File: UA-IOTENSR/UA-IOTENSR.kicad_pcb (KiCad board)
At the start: 2 copper layers, 26 parts, among them IC201 BQ2000TPN-B5, J1 Conn_01x04_Male, J201 ZX62-AB-5PA_31_, J202 S2B-ZR-SM4A-TF(LF)(SN), SW1 SW_DPST, U1 ESP32-S3-MINI-1

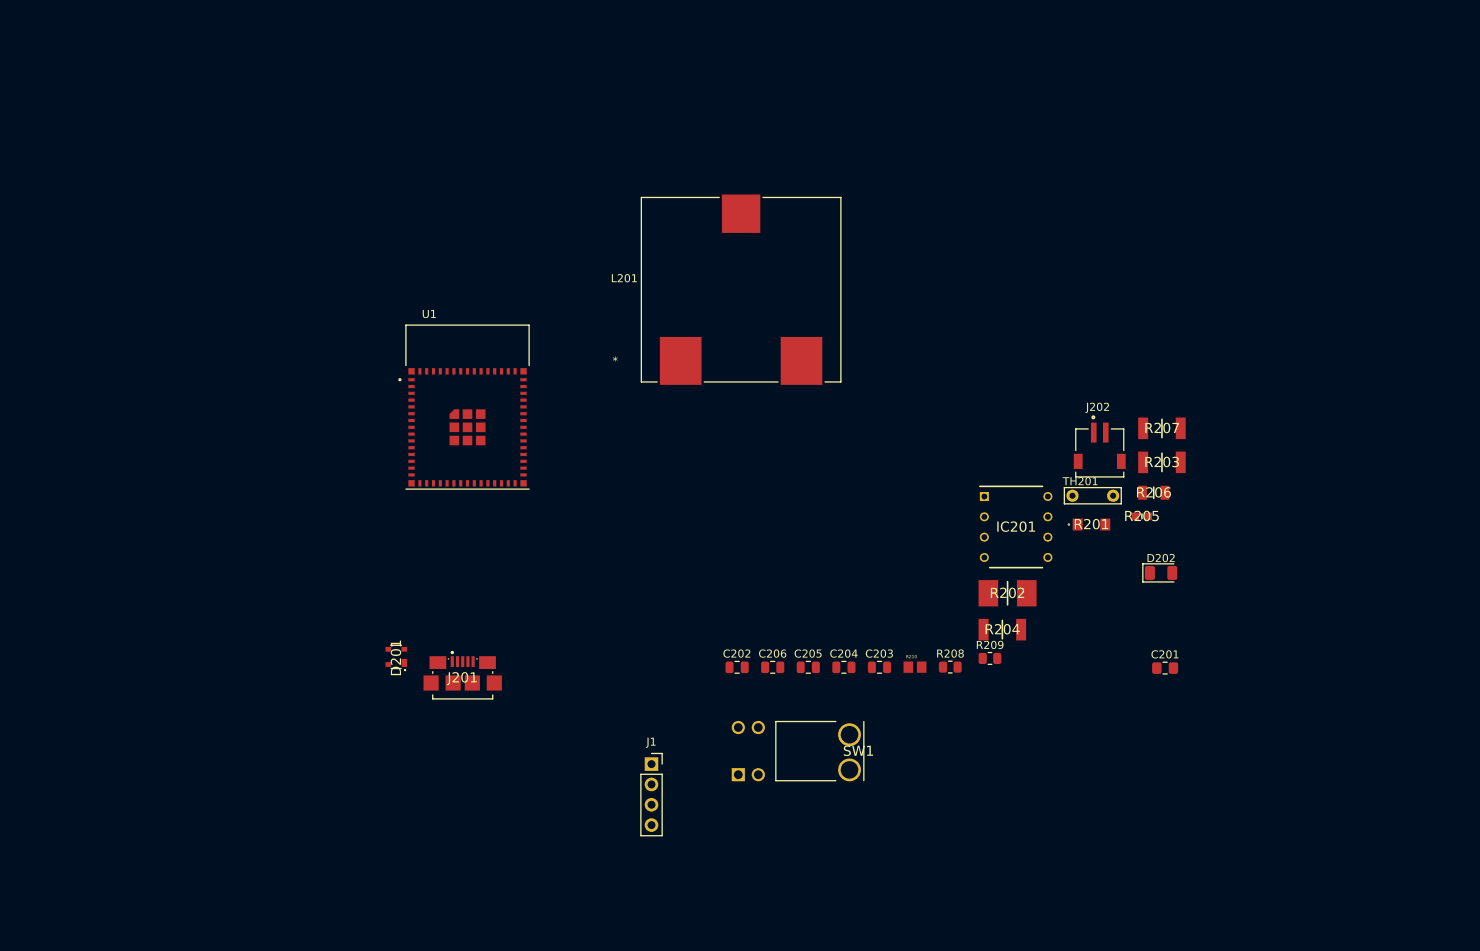
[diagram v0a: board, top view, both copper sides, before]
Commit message: Added 3V3 switch reg with footprint
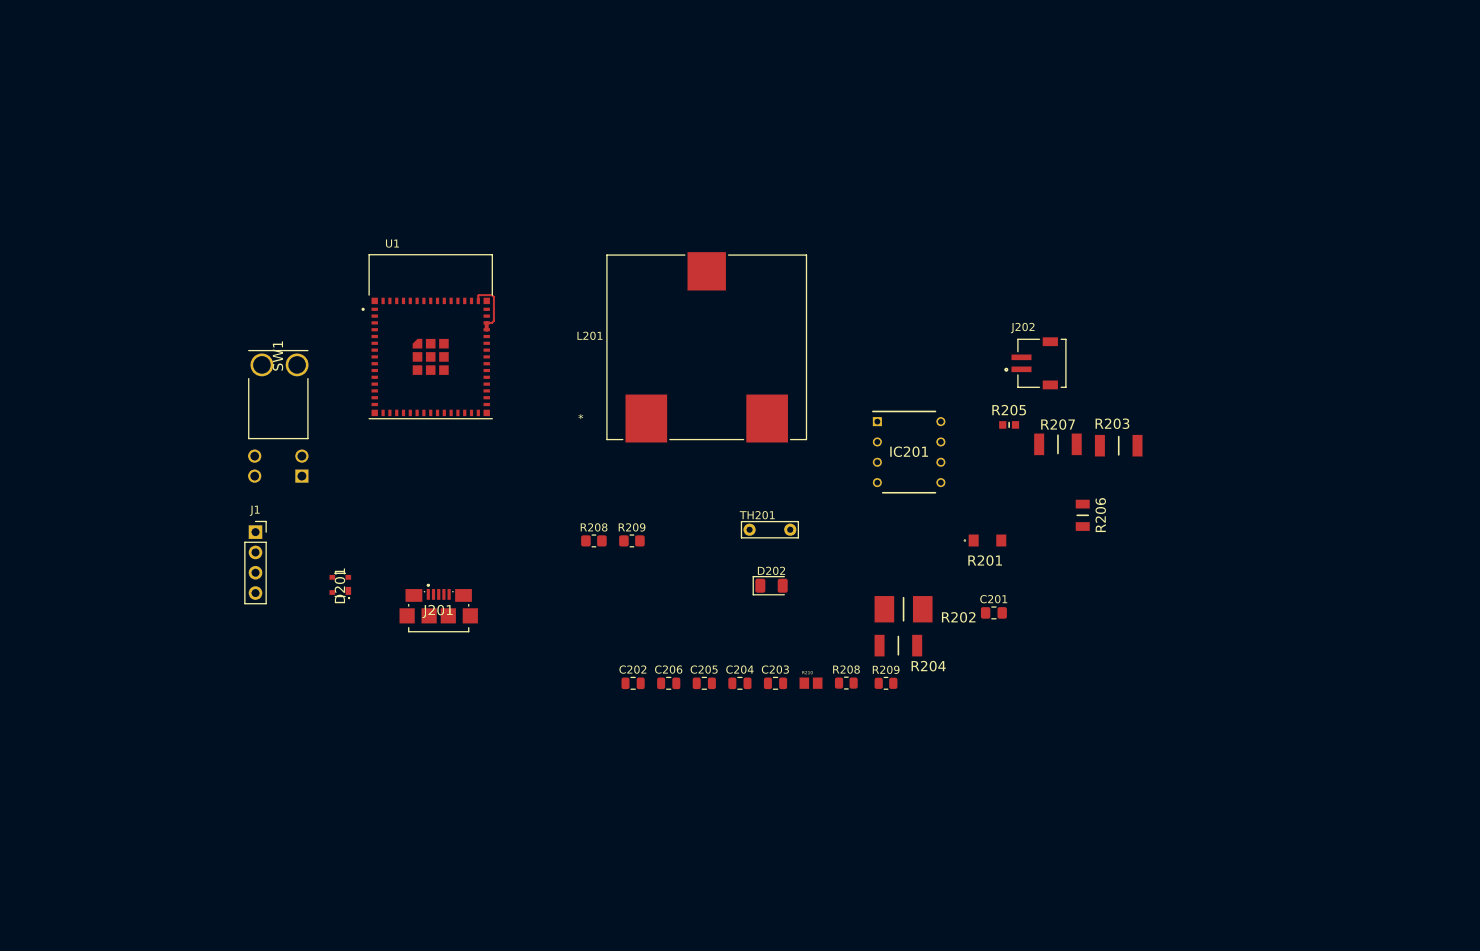
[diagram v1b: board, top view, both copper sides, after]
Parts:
- added R208: 4.8047k, Resistor_SMD:R_0805_2012Metric_Pad1.20x1.40mm_HandSolder, F.Cu at (148.8, 86.3)
- added R209: 5.7668k, Resistor_SMD:R_0805_2012Metric_Pad1.20x1.40mm_HandSolder, F.Cu at (153.6, 86.3)
- moved SW1 66.1 mm to (112.3, 78.2), turned to 90 degrees
- moved J1 57.4 mm to (106.5, 85.2)
- moved D202 48.7 mm to (171.0, 91.9)
- moved TH201 40.6 mm to (170.8, 84.9)
- moved C201 22.5 mm to (198.8, 95.3)
- moved R205 20.2 mm to (200.7, 71.8)
- moved IC201 16.3 mm to (188.2, 75.2)
- moved R209 13.4 mm to (185.3, 104.1)
- moved J202 13.2 mm to (204.4, 64.1), turned to 90 degrees
- moved C202 13.2 mm to (153.7, 104.1)
- moved C203 13.2 mm to (171.5, 104.1)
- moved C204 13.2 mm to (167.1, 104.1)
- moved C205 13.2 mm to (162.6, 104.1)
- moved C206 13.2 mm to (158.2, 104.1)
- moved R201 13.2 mm to (198.0, 86.2)
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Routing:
- net BAT-: track 0.00 -> 7.57 mm

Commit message: Completed regulator circuit; switched to 4-layer board setup
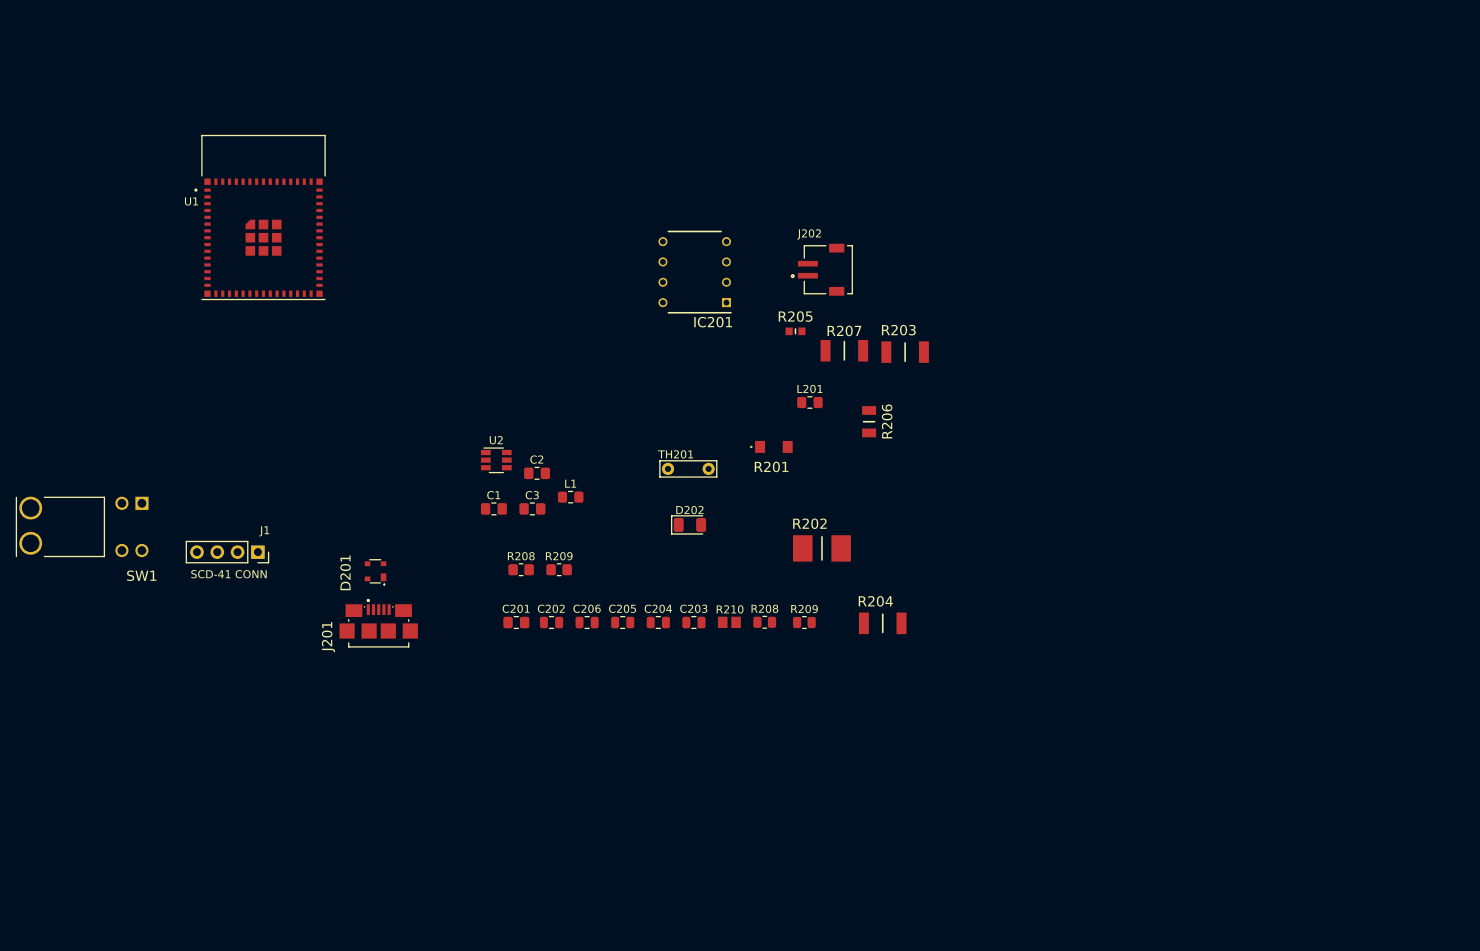
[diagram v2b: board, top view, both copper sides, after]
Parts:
- added C1: 10u, Capacitor_SMD:C_0805_2012Metric_Pad1.18x1.45mm_HandSolder, F.Cu at (136.3, 82.3)
- added C2: 100n, Capacitor_SMD:C_0805_2012Metric_Pad1.18x1.45mm_HandSolder, F.Cu at (141.7, 77.8)
- added C3: 44u, Capacitor_SMD:C_0805_2012Metric_Pad1.18x1.45mm_HandSolder, F.Cu at (141.1, 82.3)
- added L1: 2.2u, Inductor_SMD:L_0805_2012Metric_Pad1.15x1.40mm_HandSolder, F.Cu at (145.9, 80.8)
- added U2: AP63203WU, Package_TO_SOT_SMD:TSOT-23-6, F.Cu at (136.6, 76.2)
- L201: footprint 30u_inductor:B82559A0303A024 -> Inductor_SMD:L_0805_2012Metric_Pad1.15x1.40mm_HandSolder
- moved C201 59.7 mm to (139.1, 96.5)
- moved IC201 35.0 mm to (161.4, 52.7), turned to 180 degrees
- moved R201 29.2 mm to (171.3, 74.5)
- moved R203 29.2 mm to (187.7, 62.7)
- moved R207 29.2 mm to (180.1, 62.5)
- moved J202 29.2 mm to (177.7, 52.4)
- moved R206 29.2 mm to (183.2, 71.4)
- moved R205 29.2 mm to (174.0, 60.1)
- moved U1 25.7 mm to (107.5, 48.4)
- moved SW1 20.3 mm to (92.3, 81.6), turned to 180 degrees
- moved L201 14.6 mm to (175.8, 69.0)
- moved TH201 12.7 mm to (160.6, 77.3)
- moved C204 12.7 mm to (156.8, 96.5)
- moved C206 12.7 mm to (147.9, 96.5)
- moved D202 12.7 mm to (160.8, 84.3)
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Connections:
- J1 pad 3: SCL -> SDA
- J1 pad 4: SDA -> SCL
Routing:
- net BAT-: track 7.57 -> 0.00 mm
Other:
- copper layers 2 -> 4
- board text added: "SCD-41 CONN"

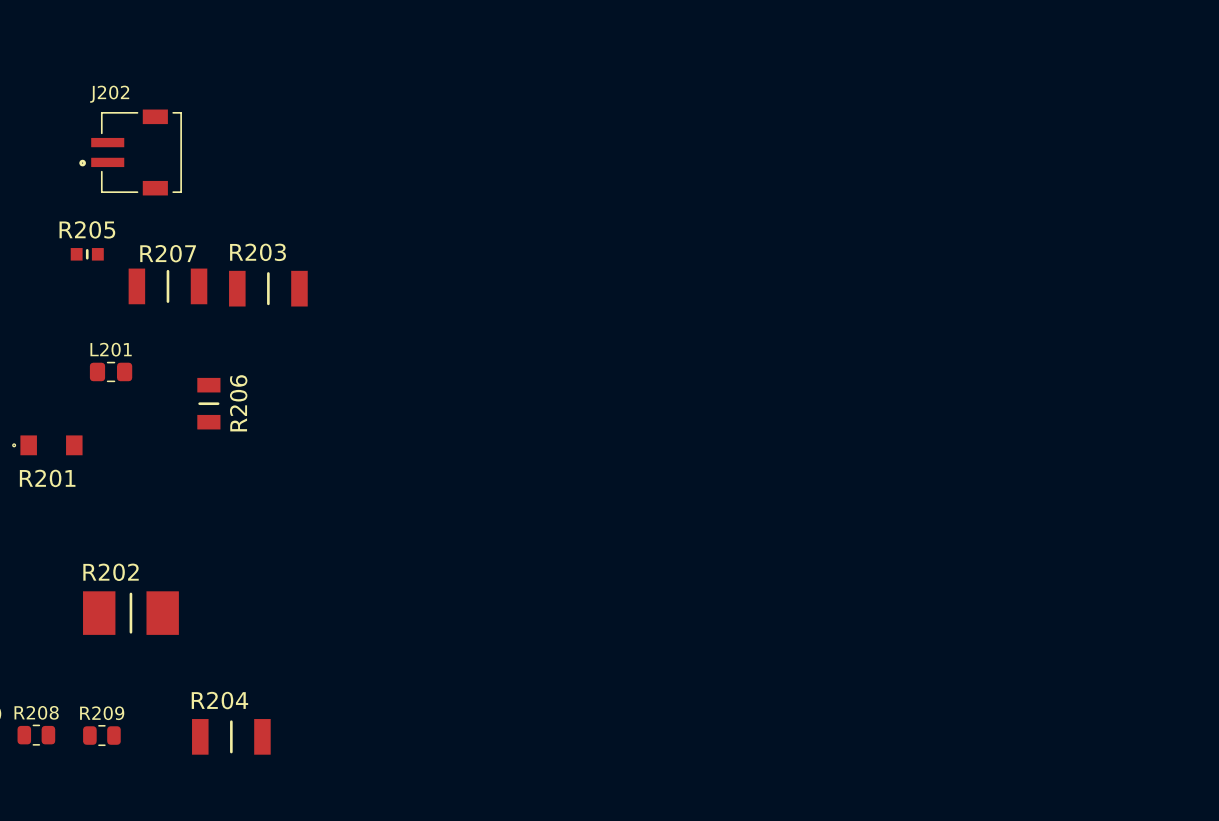
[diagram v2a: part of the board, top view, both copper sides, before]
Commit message: Switched JST Conn to Battery Holder 3x AA
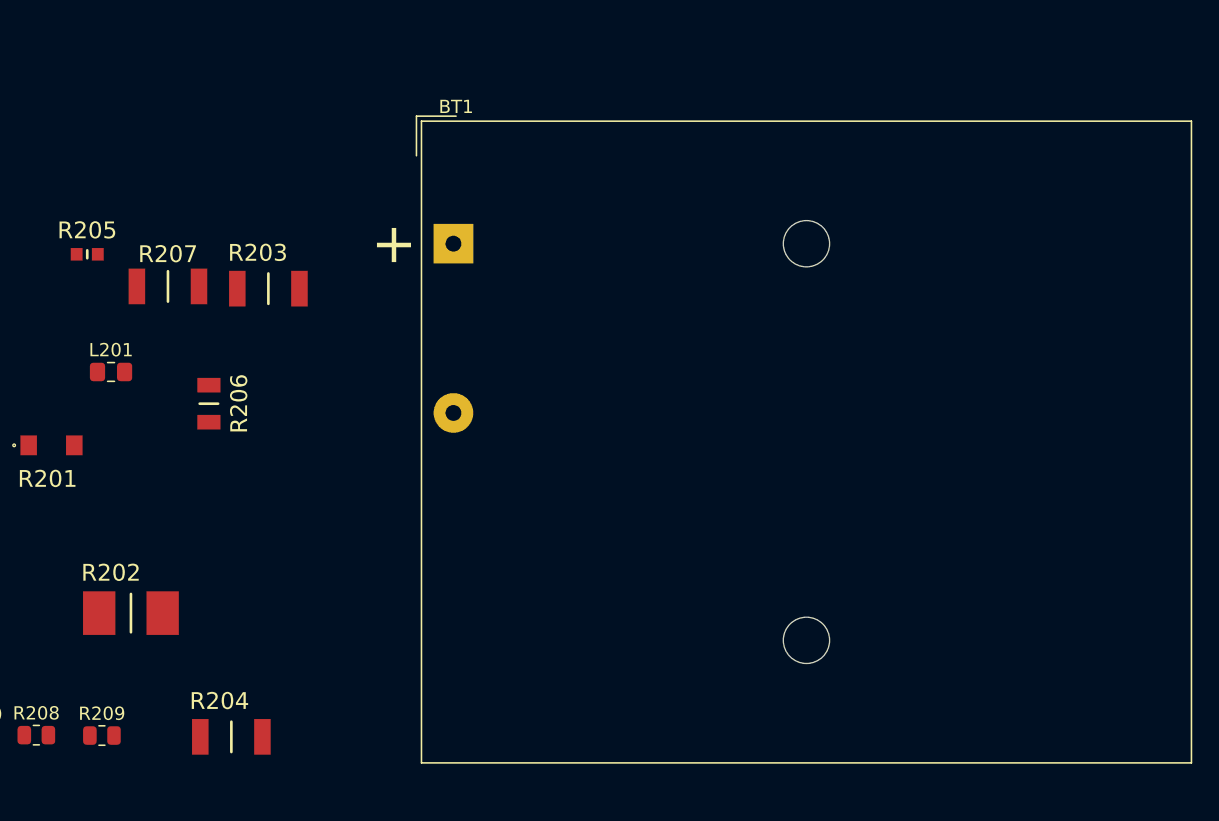
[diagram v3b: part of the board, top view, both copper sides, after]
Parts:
- removed J202: S2B-ZR-SM4A-TF(LF)(SN), JSTConns:JST_S2B-ZR-SM4A-TF(LF)(SN)
- added BT1: Battery, Battery:BatteryHolder_TruPower_BH-331P_3xAA, F.Cu at (201.7, 59.3)

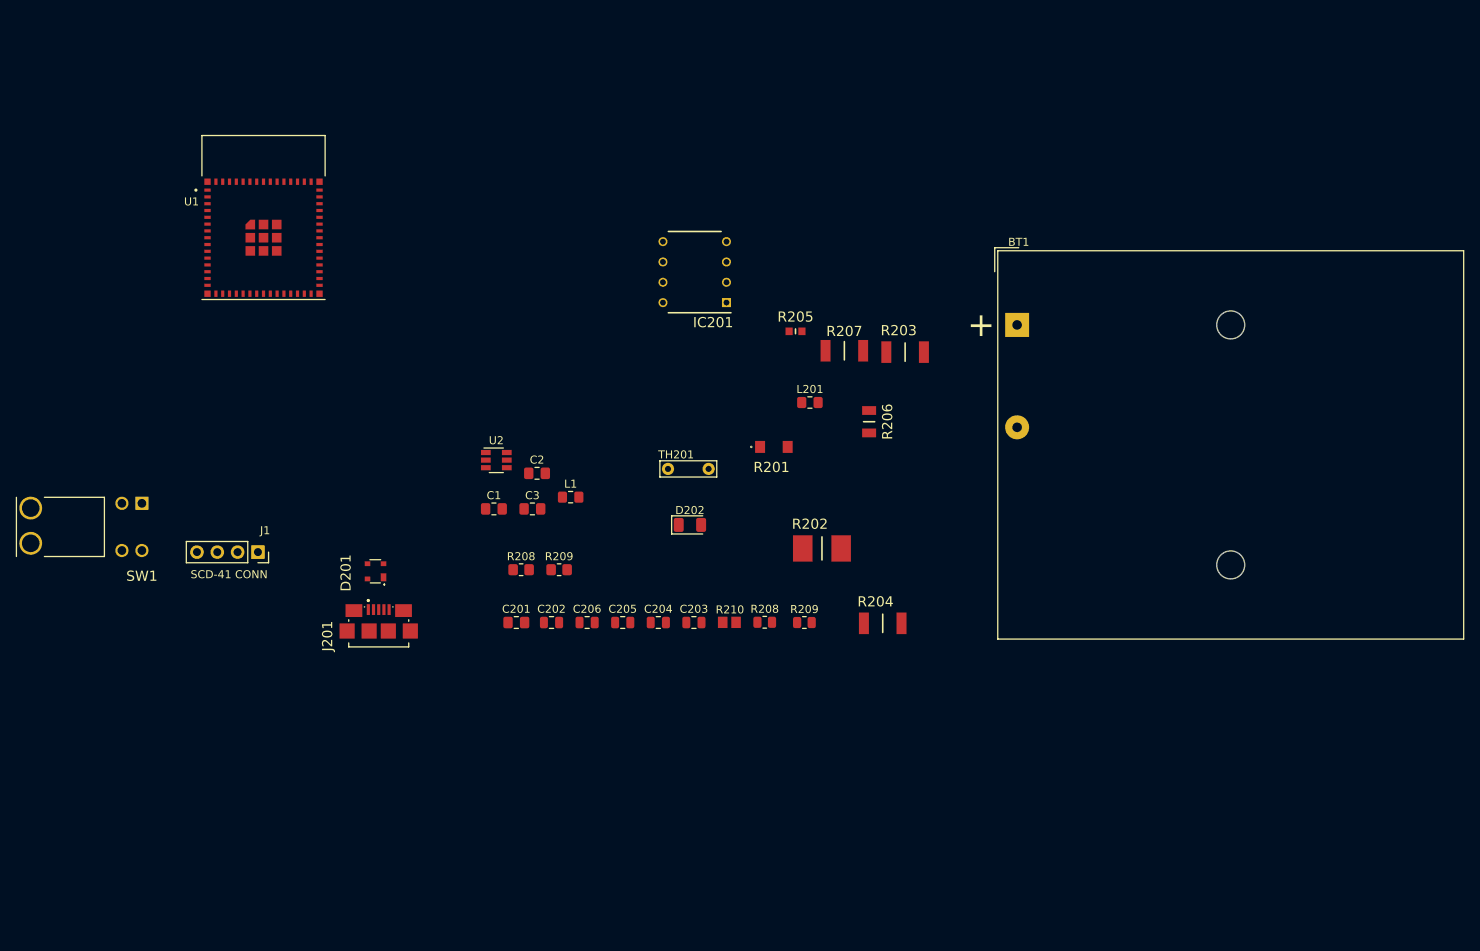
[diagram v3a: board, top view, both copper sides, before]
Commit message: Re-annotated schem, progress on layout
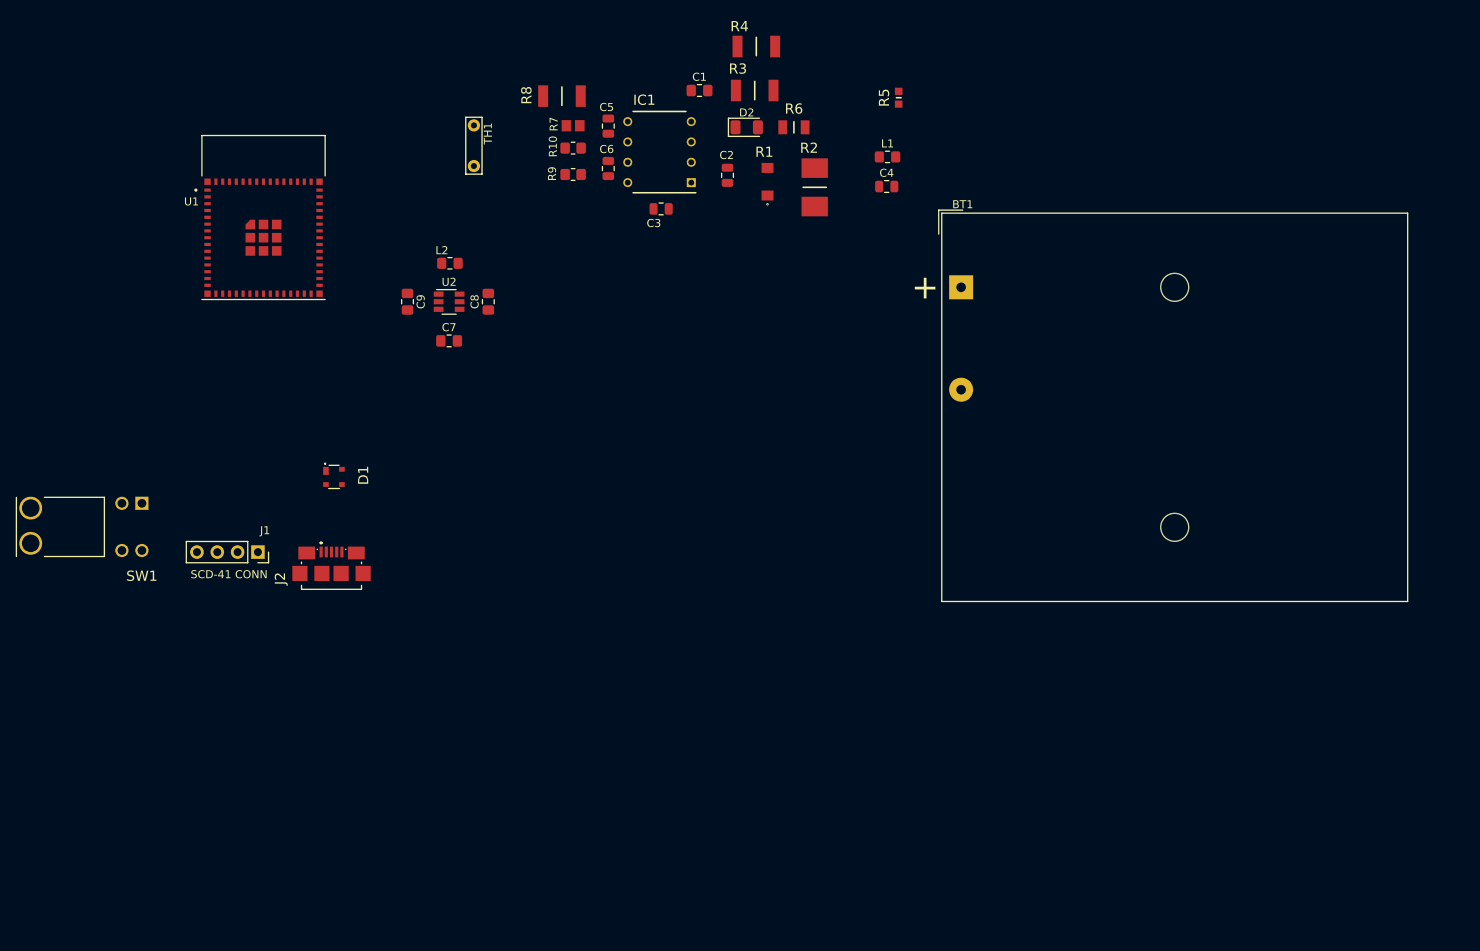
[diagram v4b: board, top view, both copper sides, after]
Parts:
- removed R208: R_T1, Resistor_SMD:R_0805_2012Metric
- removed R209: R_T2, Resistor_SMD:R_0805_2012Metric
- moved R4 73.8 mm to (169.1, 24.5)
- moved C1 70.3 mm to (162.0, 30.0)
- moved R7 65.1 mm to (146.2, 34.4), turned to 180 degrees
- moved C5 62.1 mm to (150.6, 34.5), turned to 270 degrees
- moved C4 61.5 mm to (185.4, 42.0)
- moved C2 60.1 mm to (165.5, 40.6), turned to 90 degrees
- moved C6 56.8 mm to (150.6, 39.8), turned to 90 degrees
- moved R10 52.7 mm to (146.2, 37.2)
- moved C3 51.9 mm to (157.2, 44.8)
- moved D2 50.2 mm to (167.9, 34.6)
- moved R9 49.8 mm to (146.2, 40.5), turned to 180 degrees
- moved TH1 48.5 mm to (133.8, 36.9), turned to 270 degrees
- moved R8 47.5 mm to (144.8, 30.7)
- moved R2 45.1 mm to (176.4, 42.1), turned to 90 degrees
- moved R6 38.0 mm to (173.8, 34.6), turned to 180 degrees
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- renumbered C201 to C1, C202 to C2, C203 to C3, C204 to C4, C206 to C5, C205 to C6, C1 to C7, C2 to C8, C3 to C9, D201 to D1, D202 to D2, IC201 to IC1, J201 to J2, L201 to L1, L1 to L2, R201 to R1, R209 to R10, R202 to R2, R203 to R3, R204 to R4, R205 to R5, R206 to R6, R210 to R7, R207 to R8, R208 to R9, TH201 to TH1
